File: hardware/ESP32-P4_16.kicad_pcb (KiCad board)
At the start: 2 copper layers, 151.1 x 93.4 mm, 99 parts, among them J1 String1, J10 String10, J11 String11, J12 String12, J13 String13, J14 String14, J15 String15, J16 String16, J17 Power In Left, J18 Power In Right, J19 GPIO, J2 String2, J22 DMX1, J26 OLED, J27 Aux Pwr, J28 VIN Select, J3 String3, J4 String4, J5 String5, J6 String6, J7 String7, J8 String8, J9 String9, SW1 Enter BTN, SW2 Down BTN, U1 ESP32-P4-ETH, U2 L7805, U4 74HCT541, U5 UA9638CP, U6 74HCT541, U7 LMR38020SDDAR

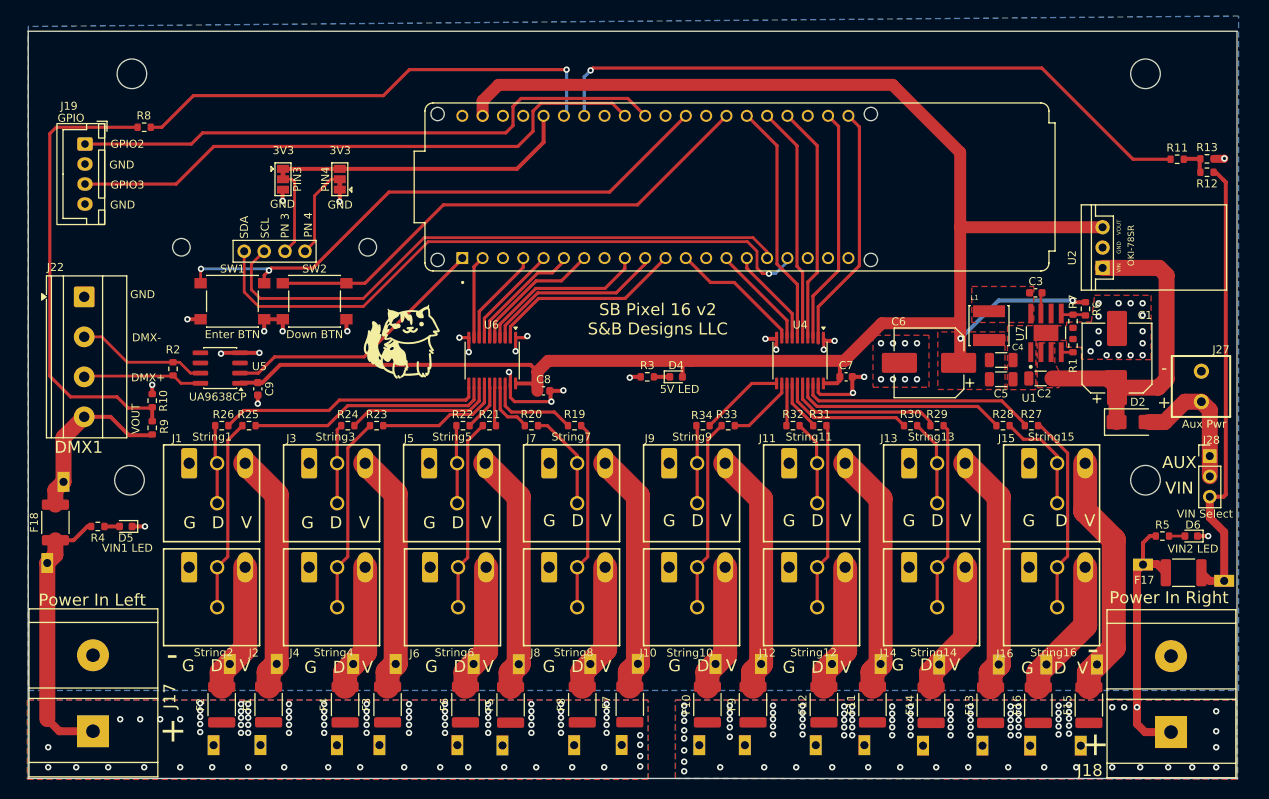
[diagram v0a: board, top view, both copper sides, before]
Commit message: update to new connectors
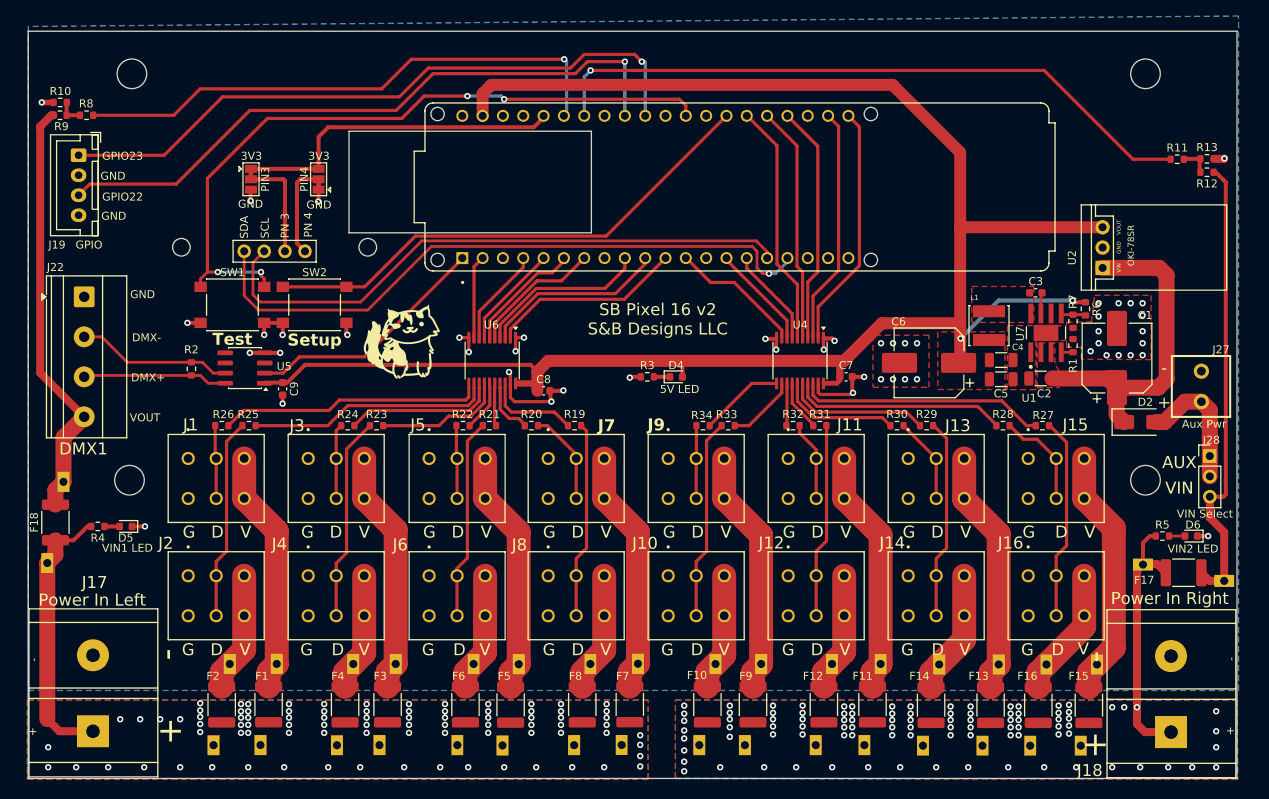
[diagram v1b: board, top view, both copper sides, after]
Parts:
- J1, J10, J11, J12, J13, J14, J15, J16, J2, J3, J4, J5, J6, J7, J8, J9: footprint Scotts:DG250-3.5-03P -> 1864299:PHOENIX_1864299_1
- SW1: value Enter BTN -> Test
- SW2: value Down BTN -> Setup
- moved R9 40.7 mm to (72.4, 71.5), turned to 0 degrees
- moved R10 39.0 mm to (72.5, 69.9), turned to 180 degrees
- moved J2 9.43 mm to (86.0, 137.1)
- moved J4 9.43 mm to (101.0, 137.1)
- moved J10 9.43 mm to (146.0, 137.1)
- moved J12 9.43 mm to (161.0, 137.1)
- moved J14 9.43 mm to (176.0, 137.1)
- moved J16 9.43 mm to (191.0, 137.1)
- moved J6 9.43 mm to (116.1, 137.1)
- moved J8 9.43 mm to (131.0, 137.1)
- moved J1 7.85 mm to (86.0, 122.4)
- moved J3 7.85 mm to (101.0, 122.4)
- moved J11 7.85 mm to (161.0, 122.4)
- moved J13 7.85 mm to (176.0, 122.4)
- moved J15 7.85 mm to (191.0, 122.4)
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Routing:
- net Net-(R10-Pad1): track 57.9 -> 3.29 mm
- net V_DMX: track 22.0 -> 53.3 mm
- net BTN1: track 72.4 -> 88.5 mm, vias 2 -> 4
- net GPIO23: track 74.7 -> 83.1 mm, vias 0 -> 1
- net VIN1_ADC: track 60.9 -> 69.1 mm
- net GPIO22: track 73.8 -> 82.0 mm, vias 0 -> 1
- net +3V3: track 37.3 -> 41.8 mm
- net TXD1: track 33.8 -> 30.7 mm
- net /Serial/DMX1-: track 16.4 -> 19.5 mm
- net /Serial/DMX1+: track 15.0 -> 18.1 mm
- net /Pin3: track 10.7 -> 13.1 mm
- net +5V: track 236.0 -> 234.2 mm
- net Net-(U4-Y3): track 16.8 -> 15.1 mm
- net /Output 9-16/DOUT12: track 23.3 -> 25.0 mm
- net /Output 9-16/DOUT14: track 23.5 -> 25.0 mm
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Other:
- outline, holes or cut-outs redrawn
- board text added: "GPIO22"
- board text added: "GPIO23"
- board text removed: "GPIO2"
- board text removed: "GPIO3"
